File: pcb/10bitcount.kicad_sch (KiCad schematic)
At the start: 3 parts

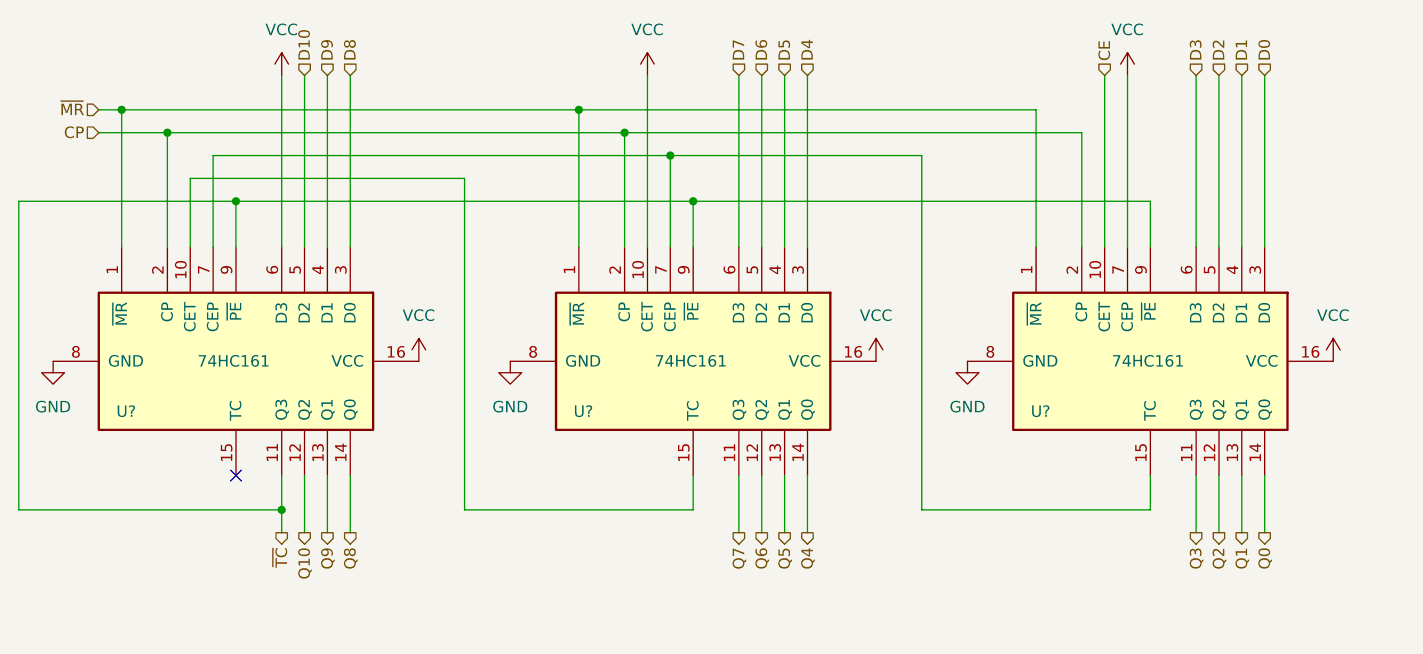
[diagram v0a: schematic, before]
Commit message: schematic: video signals, address counter, extra registers
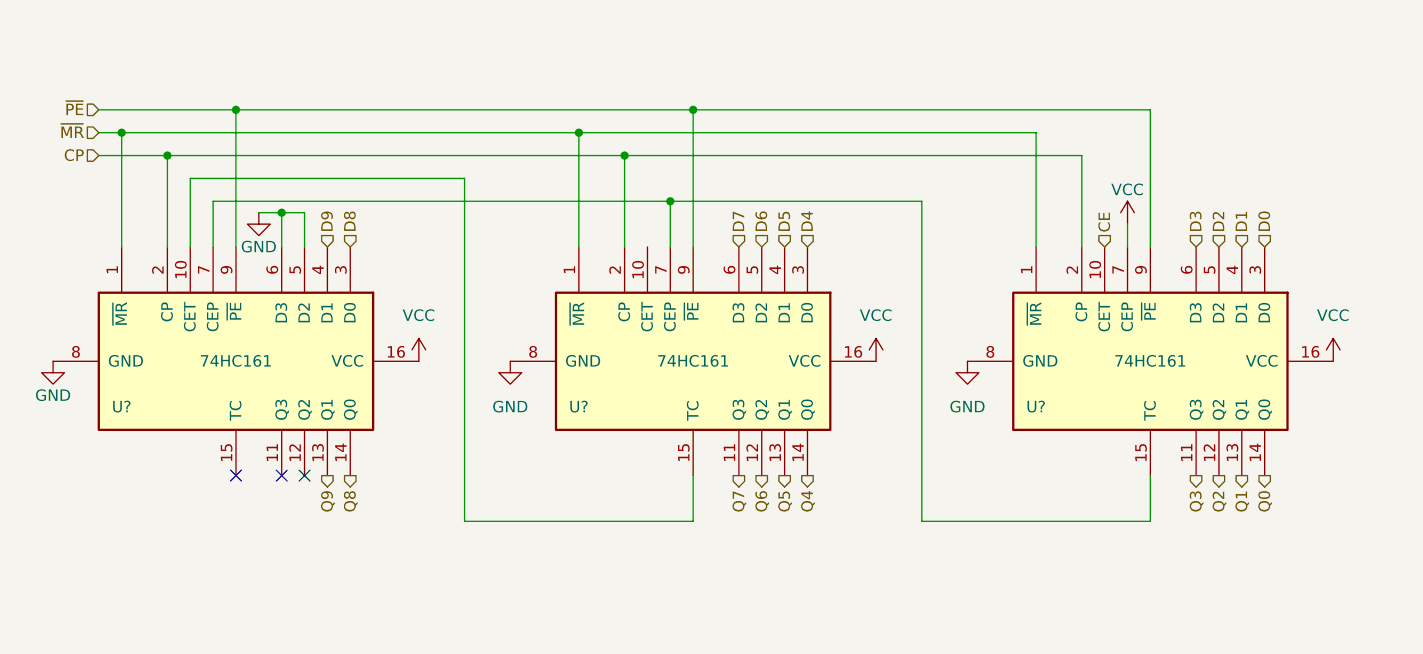
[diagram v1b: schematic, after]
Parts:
- removed U? (x3): 74HC161, symbol 74xx:74LS161
- added U? (x3): 74HC161, symbol 74xx:74LS161
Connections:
- net CE: now also U?.10 (CET)
- net CP: now also U?.2 (CP), U?.2 (CP), U?.2 (CP)
- net D0: now also U?.3 (D0)
- net D1: now also U?.4 (D1)
- net D2: now also U?.5 (D2)
- net D3: now also U?.6 (D3)
- net D4: now also U?.3 (D0)
- net D5: now also U?.4 (D1)
- net D6: now also U?.5 (D2)
- net D7: now also U?.6 (D3)
- net D8: now also U?.3 (D0)
- net D9: now also U?.4 (D1)
- net GND: now also U?.5 (D2), U?.6 (D3), U?.8 (GND), U?.8 (GND), U?.8 (GND)
- net Q0: now also U?.14 (Q0)
- net Q1: now also U?.13 (Q1)
- net Q2: now also U?.12 (Q2)
- net Q3: now also U?.11 (Q3)
- net Q4: now also U?.14 (Q0)
- net Q5: now also U?.13 (Q1)
- net Q6: now also U?.12 (Q2)
- net Q7: now also U?.11 (Q3)
- net Q8: now also U?.14 (Q0)
- net Q9: now also U?.13 (Q1)
- net VCC: now also U?.16 (VCC), U?.16 (VCC), U?.16 (VCC), U?.7 (CEP)
- net ~{MR}: now also U?.1 (~{MR}), U?.1 (~{MR}), U?.1 (~{MR})
- new net: U?.15 (TC), U?.7 (CEP), U?.7 (CEP)
- new net: U?.10 (CET), U?.15 (TC)
- new net ~{PE}: U?.9 (~{PE}), U?.9 (~{PE}), U?.9 (~{PE})
- no-connect marks 1 -> 3

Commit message: WIP schematic
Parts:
- gave numbers to parts that had none: 3
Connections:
- net VCC renamed +5V

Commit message: WIP schematic
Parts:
- renumbered U34 to U31
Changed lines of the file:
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@@
 		(dnp no)
 		(fields_autoplaced yes)
-		(property "Reference" "#PWR0102"
+		(property "Reference" "#PWR094"
 			(at 73.66 74.93 0)
 			(effects
@@
 		(dnp no)
 		(fields_autoplaced yes)
-		(property "Reference" "#PWR0107"
+		(property "Reference" "#PWR099"
 			(at 175.26 74.93 0)
 			(effects
@@
 		(dnp no)
 		(fields_autoplaced yes)
-		(property "Reference" "#PWR0103"
+		(property "Reference" "#PWR095"
 			(at 83.82 77.47 0)
 			(effects
@@
 		(on_board yes)
 		(dnp no)
-		(property "Reference" "#PWR0100"
+		(property "Reference" "#PWR092"
 			(at 33.02 77.47 0)
 			(effects
@@
 		(dnp no)
 		(fields_autoplaced yes)
-		(property "Reference" "#PWR0105"
+		(property "Reference" "#PWR097"
 			(at 134.62 77.47 0)
 			(effects
@@
 		(dnp no)
 		(fields_autoplaced yes)
-		(property "Reference" "#PWR0104"
+		(property "Reference" "#PWR096"
 			(at 124.46 74.93 0)
 			(effects
@@
 		(on_board yes)
 		(dnp no)
-		(property "Reference" "U34"
+		(property "Reference" "U31"
 			(at 40.64 76.2 90)
 			(effects
@@
 		(on_board yes)
 		(dnp no)
-		(property "Reference" "#PWR0106"
+		(property "Reference" "#PWR098"
 			(at 152.4 59.69 0)
 			(effects

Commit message: WIP PCB
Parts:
- renumbered U33 to U?, U32 to U?, U31 to U?
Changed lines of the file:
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@@
 		(shape input)
 		(at 114.3 58.42 90)
-		(fields_autoplaced yes)
 		(effects
 			(font
@@
 		(shape input)
 		(at 149.86 58.42 90)
-		(fields_autoplaced yes)
 		(effects
 			(font
@@
 		(shape output)
 		(at 160.02 83.82 270)
-		(fields_autoplaced yes)
 		(effects
 			(font
@@
 		(shape output)
 		(at 167.64 83.82 270)
-		(fields_autoplaced yes)
 		(effects
 			(font
@@
 		(shape input)
 		(at 63.5 58.42 90)
-		(fields_autoplaced yes)
 		(effects
 			(font
@@
 		(shape output)
 		(at 116.84 83.82 270)
-		(fields_autoplaced yes)
 		(effects
 			(font
@@
 		(shape input)
 		(at 165.1 58.42 90)
-		(fields_autoplaced yes)
 		(effects
 			(font
@@
 		(shape input)
 		(at 38.1 43.18 180)
-		(fields_autoplaced yes)
 		(effects
 			(font
@@
 		(shape output)
 		(at 165.1 83.82 270)
-		(fields_autoplaced yes)
 		(effects
 			(font
@@
 		(shape output)
 		(at 114.3 83.82 270)
-		(fields_autoplaced yes)
 		(effects
 			(font
@@
 		(shape output)
 		(at 162.56 83.82 270)
-		(fields_autoplaced yes)
 		(effects
 			(font
@@
 		(shape output)
 		(at 109.22 83.82 270)
-		(fields_autoplaced yes)
 		(effects
 			(font
@@
 		(shape input)
 		(at 38.1 45.72 180)
-		(fields_autoplaced yes)
 		(effects
 			(font
@@
 		(shape output)
 		(at 63.5 83.82 270)
-		(fields_autoplaced yes)
 		(effects
 			(font
@@
 		(shape input)
 		(at 111.76 58.42 90)
-		(fields_autoplaced yes)
 		(effects
 			(font
@@
 		(shape input)
 		(at 167.64 58.42 90)
-		(fields_autoplaced yes)
 		(effects
 			(font
@@
 		(shape input)
 		(at 109.22 58.42 90)
-		(fields_autoplaced yes)
 		(effects
 			(font
@@
 		(shape input)
 		(at 160.02 58.42 90)
-		(fields_autoplaced yes)
 		(effects
 			(font
@@
 		(shape input)
 		(at 38.1 48.26 180)
-		(fields_autoplaced yes)
 		(effects
 			(font
@@
 		(shape output)
 		(at 111.76 83.82 270)
-		(fields_autoplaced yes)
 		(effects
 			(font
@@
 		(shape input)
 		(at 162.56 58.42 90)
-		(fields_autoplaced yes)
 		(effects
 			(font
@@
 		(shape output)
 		(at 66.04 83.82 270)
-		(fields_autoplaced yes)
 		(effects
 			(font
@@
 		(shape input)
 		(at 66.04 58.42 90)
-		(fields_autoplaced yes)
 		(effects
 			(font
@@
 		(shape input)
 		(at 116.84 58.42 90)
-		(fields_autoplaced yes)
 		(effects
 			(font
@@
 		(dnp no)
 		(fields_autoplaced yes)
-		(property "Reference" "#PWR094"
+		(property "Reference" "#PWR?"
 			(at 73.66 74.93 0)
 			(effects
@@
 			(project ""
 				(path "/e63e39d7-6ac0-4ffd-8aa3-1841a4541b55/90e1f016-3c60-4383-aa8d-def9977ac47b/22fed627-5774-4fe5-8536-0466d92a967a"
-					(reference "#PWR094")
+					(reference "#PWR?")
 					(unit 1)
 				)
 				(path "/e63e39d7-6ac0-4ffd-8aa3-1841a4541b55/90e1f016-3c60-4383-aa8d-def9977ac47b/6eee35b4-65a4-4e78-9eee-35747a769478"
-					(reference "#PWR0102")
+					(reference "#PWR?")
 					(unit 1)
 				)
@@
 		(dnp no)
 		(fields_autoplaced yes)
-		(property "Reference" "#PWR099"
+		(property "Reference" "#PWR?"
 			(at 175.26 74.93 0)
 			(effects
@@
 			(project ""
 				(path "/e63e39d7-6ac0-4ffd-8aa3-1841a4541b55/90e1f016-3c60-4383-aa8d-def9977ac47b/22fed627-5774-4fe5-8536-0466d92a967a"
-					(reference "#PWR099")
+					(reference "#PWR?")
 					(unit 1)
 				)
 				(path "/e63e39d7-6ac0-4ffd-8aa3-1841a4541b55/90e1f016-3c60-4383-aa8d-def9977ac47b/6eee35b4-65a4-4e78-9eee-35747a769478"
-					(reference "#PWR0107")
+					(reference "#PWR?")
 					(unit 1)
 				)
@@
 		(on_board yes)
 		(dnp no)
-		(property "Reference" "U33"
+		(property "Reference" "U?"
 			(at 142.24 76.2 90)
 			(effects
@@
 			(project "fnx51"
 				(path "/e63e39d7-6ac0-4ffd-8aa3-1841a4541b55/90e1f016-3c60-4383-aa8d-def9977ac47b/22fed627-5774-4fe5-8536-0466d92a967a"
-					(reference "U33")
+					(reference "U?")
 					(unit 1)
 				)
 				(path "/e63e39d7-6ac0-4ffd-8aa3-1841a4541b55/90e1f016-3c60-4383-aa8d-def9977ac47b/6eee35b4-65a4-4e78-9eee-35747a769478"
-					(reference "U36")
+					(reference "U?")
 					(unit 1)
 				)
@@
 		(dnp no)
 		(fields_autoplaced yes)
-		(property "Reference" "#PWR095"
+		(property "Reference" "#PWR?"
 			(at 83.82 77.47 0)
 			(effects
@@
 			(project ""
 				(path "/e63e39d7-6ac0-4ffd-8aa3-1841a4541b55/90e1f016-3c60-4383-aa8d-def9977ac47b/22fed627-5774-4fe5-8536-0466d92a967a"
-					(reference "#PWR095")
+					(reference "#PWR?")
 					(unit 1)
 				)
 				(path "/e63e39d7-6ac0-4ffd-8aa3-1841a4541b55/90e1f016-3c60-4383-aa8d-def9977ac47b/6eee35b4-65a4-4e78-9eee-35747a769478"
-					(reference "#PWR0103")
+					(reference "#PWR?")
 					(unit 1)
 				)
@@
 		(on_board yes)
 		(dnp no)
-		(property "Reference" "#PWR092"
+		(property "Reference" "#PWR?"
 			(at 33.02 77.47 0)
 			(effects
@@
 			(project ""
 				(path "/e63e39d7-6ac0-4ffd-8aa3-1841a4541b55/90e1f016-3c60-4383-aa8d-def9977ac47b/22fed627-5774-4fe5-8536-0466d92a967a"
-					(reference "#PWR092")
+					(reference "#PWR?")
 					(unit 1)
 				)
 				(path "/e63e39d7-6ac0-4ffd-8aa3-1841a4541b55/90e1f016-3c60-4383-aa8d-def9977ac47b/6eee35b4-65a4-4e78-9eee-35747a769478"
-					(reference "#PWR0100")
+					(reference "#PWR?")
 					(unit 1)
 				)
@@
 		(on_board yes)
 		(dnp no)
-		(property "Reference" "#PWR093"
+		(property "Reference" "#PWR?"
 			(at 55.88 60.96 0)
 			(effects
@@
 			(project "fnx51"
 				(path "/e63e39d7-6ac0-4ffd-8aa3-1841a4541b55/90e1f016-3c60-4383-aa8d-def9977ac47b/22fed627-5774-4fe5-8536-0466d92a967a"
-					(reference "#PWR093")
+					(reference "#PWR?")
 					(unit 1)
 				)
 				(path "/e63e39d7-6ac0-4ffd-8aa3-1841a4541b55/90e1f016-3c60-4383-aa8d-def9977ac47b/6eee35b4-65a4-4e78-9eee-35747a769478"
-					(reference "#PWR0101")
+					(reference "#PWR?")
 					(unit 1)
 				)
@@
 		(dnp no)
 		(fields_autoplaced yes)
-		(property "Reference" "#PWR097"
+		(property "Reference" "#PWR?"
 			(at 134.62 77.47 0)
 			(effects
@@
 			(project ""
 				(path "/e63e39d7-6ac0-4ffd-8aa3-1841a4541b55/90e1f016-3c60-4383-aa8d-def9977ac47b/22fed627-5774-4fe5-8536-0466d92a967a"
-					(reference "#PWR097")
+					(reference "#PWR?")
 					(unit 1)
 				)
 				(path "/e63e39d7-6ac0-4ffd-8aa3-1841a4541b55/90e1f016-3c60-4383-aa8d-def9977ac47b/6eee35b4-65a4-4e78-9eee-35747a769478"
-					(reference "#PWR0105")
+					(reference "#PWR?")
 					(unit 1)
 				)
@@
 		(on_board yes)
 		(dnp no)
-		(property "Reference" "U32"
+		(property "Reference" "U?"
 			(at 91.44 76.2 90)
 			(effects
@@
 			(project "fnx51"
 				(path "/e63e39d7-6ac0-4ffd-8aa3-1841a4541b55/90e1f016-3c60-4383-aa8d-def9977ac47b/22fed627-5774-4fe5-8536-0466d92a967a"
-					(reference "U32")
+					(reference "U?")
 					(unit 1)
 				)
 				(path "/e63e39d7-6ac0-4ffd-8aa3-1841a4541b55/90e1f016-3c60-4383-aa8d-def9977ac47b/6eee35b4-65a4-4e78-9eee-35747a769478"
-					(reference "U35")
+					(reference "U?")
 					(unit 1)
 				)
@@
 		(dnp no)
 		(fields_autoplaced yes)
-		(property "Reference" "#PWR096"
+		(property "Reference" "#PWR?"
 			(at 124.46 74.93 0)
 			(effects
@@
 			(project ""
 				(path "/e63e39d7-6ac0-4ffd-8aa3-1841a4541b55/90e1f016-3c60-4383-aa8d-def9977ac47b/22fed627-5774-4fe5-8536-0466d92a967a"
-					(reference "#PWR096")
+					(reference "#PWR?")
 					(unit 1)
 				)
 				(path "/e63e39d7-6ac0-4ffd-8aa3-1841a4541b55/90e1f016-3c60-4383-aa8d-def9977ac47b/6eee35b4-65a4-4e78-9eee-35747a769478"
-					(reference "#PWR0104")
+					(reference "#PWR?")
 					(unit 1)
 				)
@@
 		(on_board yes)
 		(dnp no)
-		(property "Reference" "U31"
+		(property "Reference" "U?"
 			(at 40.64 76.2 90)
 			(effects
@@
 			(project ""
 				(path "/e63e39d7-6ac0-4ffd-8aa3-1841a4541b55/90e1f016-3c60-4383-aa8d-def9977ac47b/22fed627-5774-4fe5-8536-0466d92a967a"
-					(reference "U31")
+					(reference "U?")
 					(unit 1)
 				)
 				(path "/e63e39d7-6ac0-4ffd-8aa3-1841a4541b55/90e1f016-3c60-4383-aa8d-def9977ac47b/6eee35b4-65a4-4e78-9eee-35747a769478"
-					(reference "U34")
+					(reference "U?")
 					(unit 1)
 				)
@@
 		(on_board yes)
 		(dnp no)
-		(property "Reference" "#PWR098"
+		(property "Reference" "#PWR?"
 			(at 152.4 59.69 0)
 			(effects
@@
 			(project ""
 				(path "/e63e39d7-6ac0-4ffd-8aa3-1841a4541b55/90e1f016-3c60-4383-aa8d-def9977ac47b/22fed627-5774-4fe5-8536-0466d92a967a"
-					(reference "#PWR098")
+					(reference "#PWR?")
 					(unit 1)
 				)
 				(path "/e63e39d7-6ac0-4ffd-8aa3-1841a4541b55/90e1f016-3c60-4383-aa8d-def9977ac47b/6eee35b4-65a4-4e78-9eee-35747a769478"
-					(reference "#PWR0106")
-					(unit 1)
-				)
+					(reference "#PWR?")
+					(unit 1)
+				)
